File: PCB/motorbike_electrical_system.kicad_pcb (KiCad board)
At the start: 2 copper layers, 116.9 x 83.4 mm, 103 parts, among them IC2 BDX34C, IC3 BDX34C, K1 RT42xxxx, Q1 D45VH10, Q10 BC337, Q11 BC337, Q12 BC327, Q13 BC337, Q14 D45VH10, Q15 D45VH10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

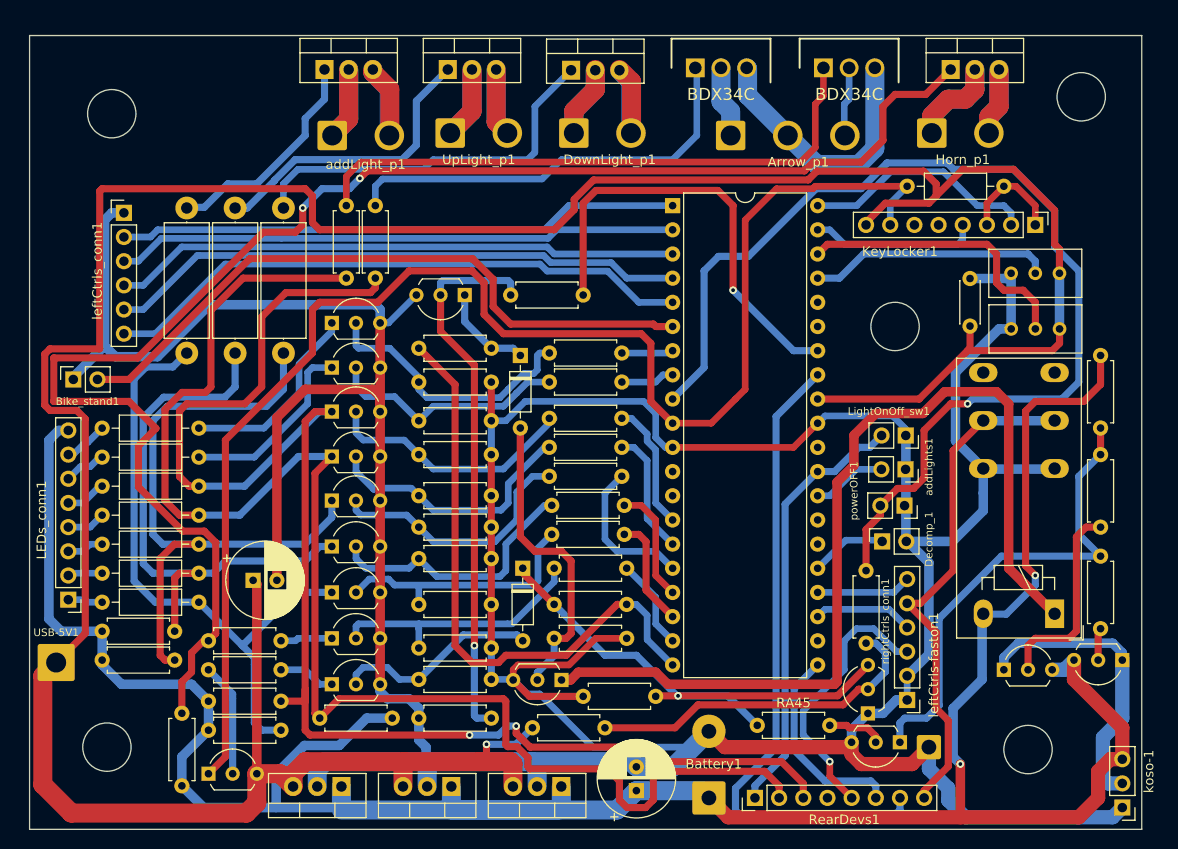
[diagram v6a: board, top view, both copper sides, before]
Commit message: RS232 connector added for debug purples
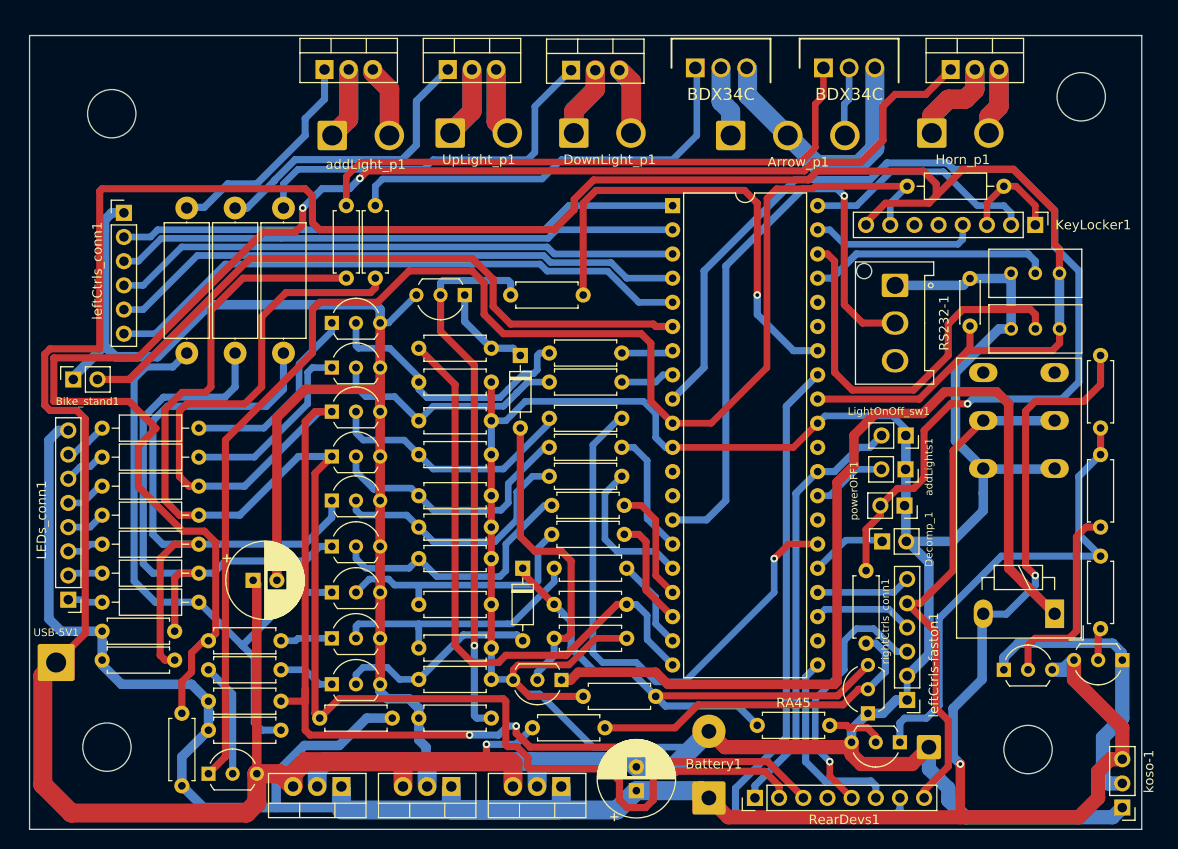
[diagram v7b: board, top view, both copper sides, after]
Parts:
- added RS232-1: Conn_01x03, Connector_Hirose:Hirose_DF63M-3P-3.96DSA_1x03_P3.96mm_Vertical, F.Cu at (190.5, 81.9)
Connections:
- U4 pad 14: o_rightArrow -> Net-(U4-Pad14)
- U4 pad 26: unconnected-(U4-Pad26) -> o_rightArrow
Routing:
- net Net-(U4-Pad14): track 0.00 -> 64.8 mm, vias 0 -> 1
- net o_rightArrow: track 13.5 -> 58.8 mm, vias 0 -> 1
- net Net-(RV1-Pad2): track 30.4 -> 42.8 mm
- net GND: track 466.3 -> 474.5 mm
- net Net-(D4-Pad1): track 54.9 -> 56.6 mm, vias 1 -> 0
- net o_engineOFF: track 47.0 -> 48.7 mm
- net c_brakeSwitch: track 28.5 -> 27.5 mm
- net o_startEngine: track 21.4 -> 20.4 mm
- net c_rightArrow: track 154.7 -> 153.8 mm
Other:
- outline, holes or cut-outs redrawn

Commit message: RS232 TxD line added
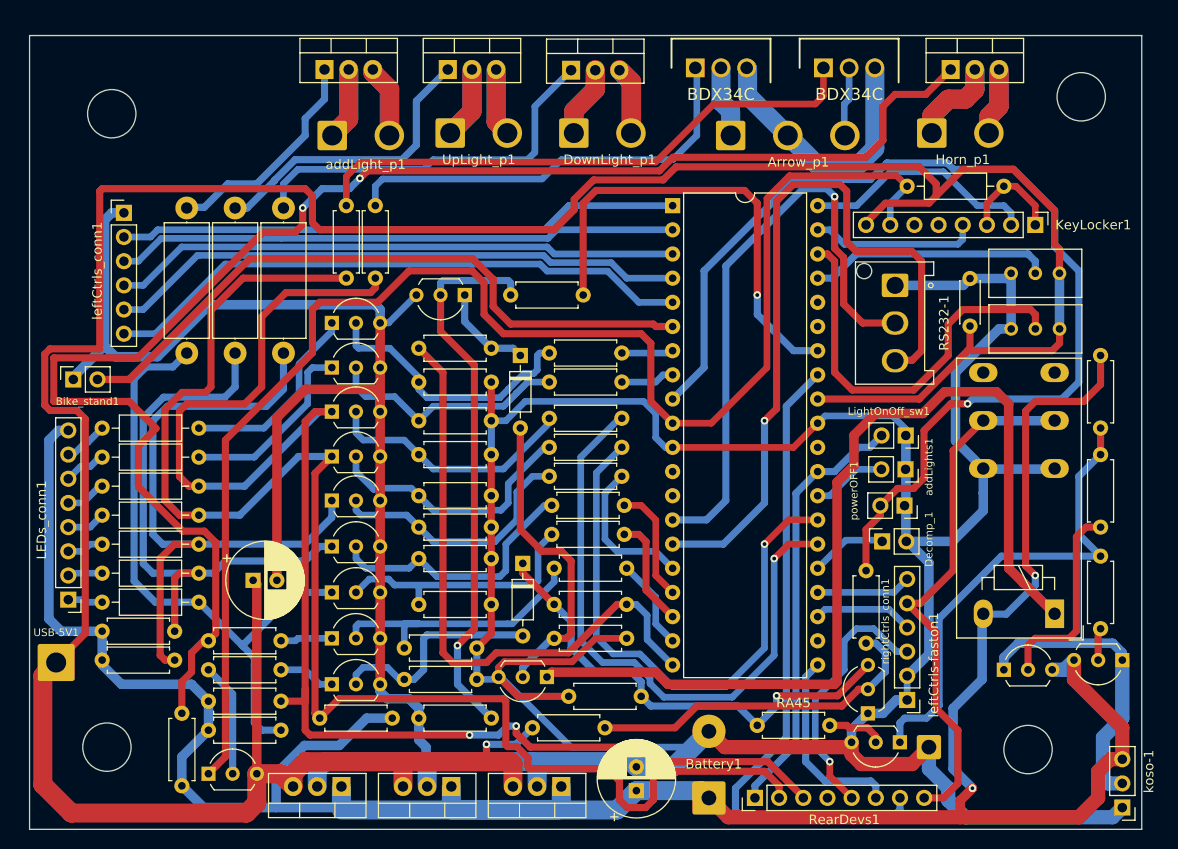
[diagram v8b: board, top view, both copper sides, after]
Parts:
- moved Q13 1.57 mm to (153.9, 123.1)
- moved RA30 1.52 mm to (138.9, 123.3)
- moved RA32 1.52 mm to (138.9, 120.0)
- moved RA48 1.52 mm to (163.8, 125.1)
- moved D4 0.51 mm to (151.4, 111.1)
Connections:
- RS232-1 pad 3: unconnected-(RS232-1-Pad3) -> Net-(U4-Pad15)
- U4 pad 15: o_leftArrow -> Net-(U4-Pad15)
- U4 pad 27: unconnected-(U4-Pad27) -> o_leftArrow
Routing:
- net Net-(U4-Pad15): track 0.00 -> 78.8 mm, vias 0 -> 1
- net o_leftArrow: track 13.1 -> 60.1 mm, vias 0 -> 1
- net Net-(D4-Pad1): track 56.6 -> 49.7 mm, vias 0 -> 1
- net o_rightArrow: track 58.8 -> 65.3 mm
- net GND: track 474.5 -> 478.3 mm
- net Net-(IC2-Pad1): track 62.3 -> 59.6 mm
- net c_engineOFF: track 54.1 -> 56.2 mm
- net Net-(D4-Pad2): track 21.6 -> 23.3 mm
- net Net-(Q9-Pad2): track 28.0 -> 29.5 mm
- net Net-(K1-PadA1): track 99.3 -> 100.7 mm
- net o_keepAlive: track 63.1 -> 64.3 mm
- net +12V: track 272.1 -> 273.1 mm
- net tempPower: track 155.1 -> 156.0 mm
- net Net-(RS232-1-Pad2): track 64.8 -> 64.1 mm
- net Net-(Q17-Pad2): track 57.7 -> 58.2 mm
